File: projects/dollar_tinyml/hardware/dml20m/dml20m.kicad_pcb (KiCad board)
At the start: 2 copper layers, 40 x 20 mm, 37 parts, among them J1 USB_A, J2 Conn_ARM_SWD_TagConnect_TC203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, J3 Header 2.54mm, J4 Header 2.54mm, Q1 BC547B, SW1 SW_Push, U1 LIS2DH12, U2 LP4054HB5F, U3 PY32F003F18U6TR, U4 XC6206PxxxMR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

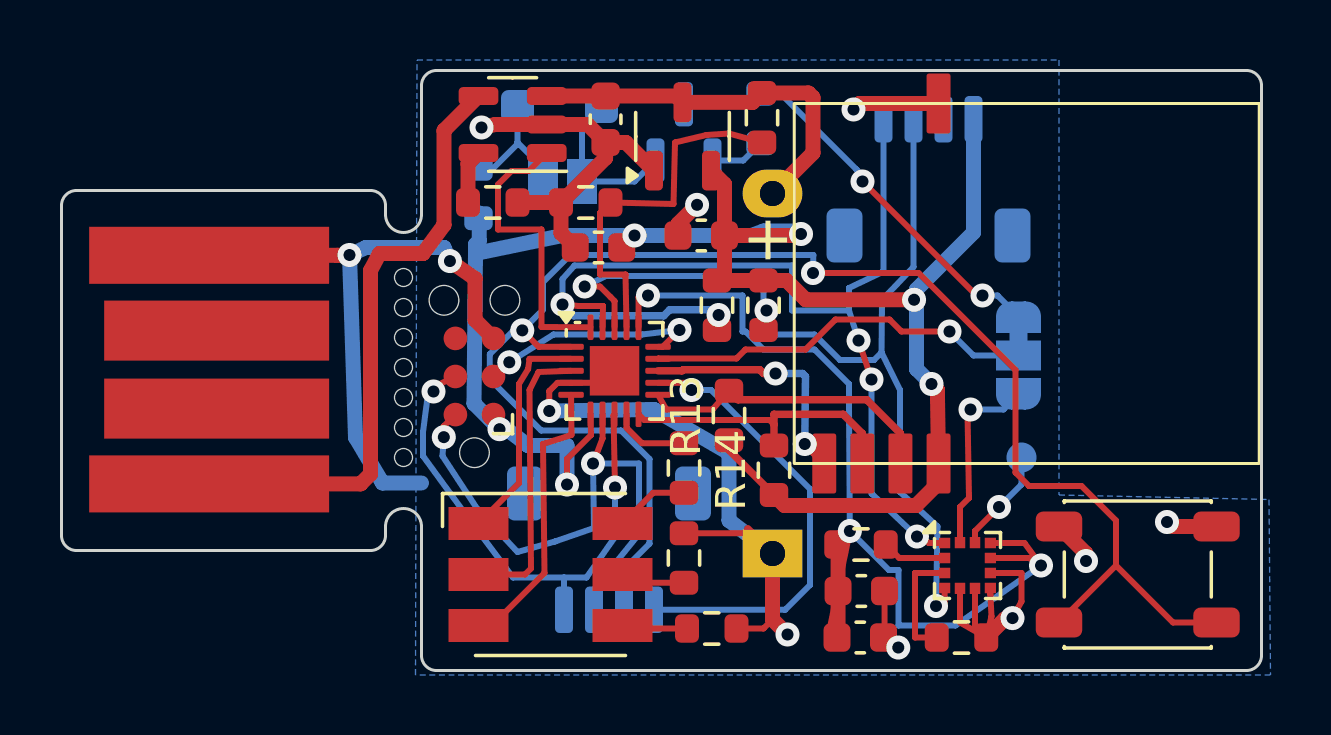
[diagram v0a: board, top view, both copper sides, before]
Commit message: dollarml: Improve groundplane, remove via-in-pad
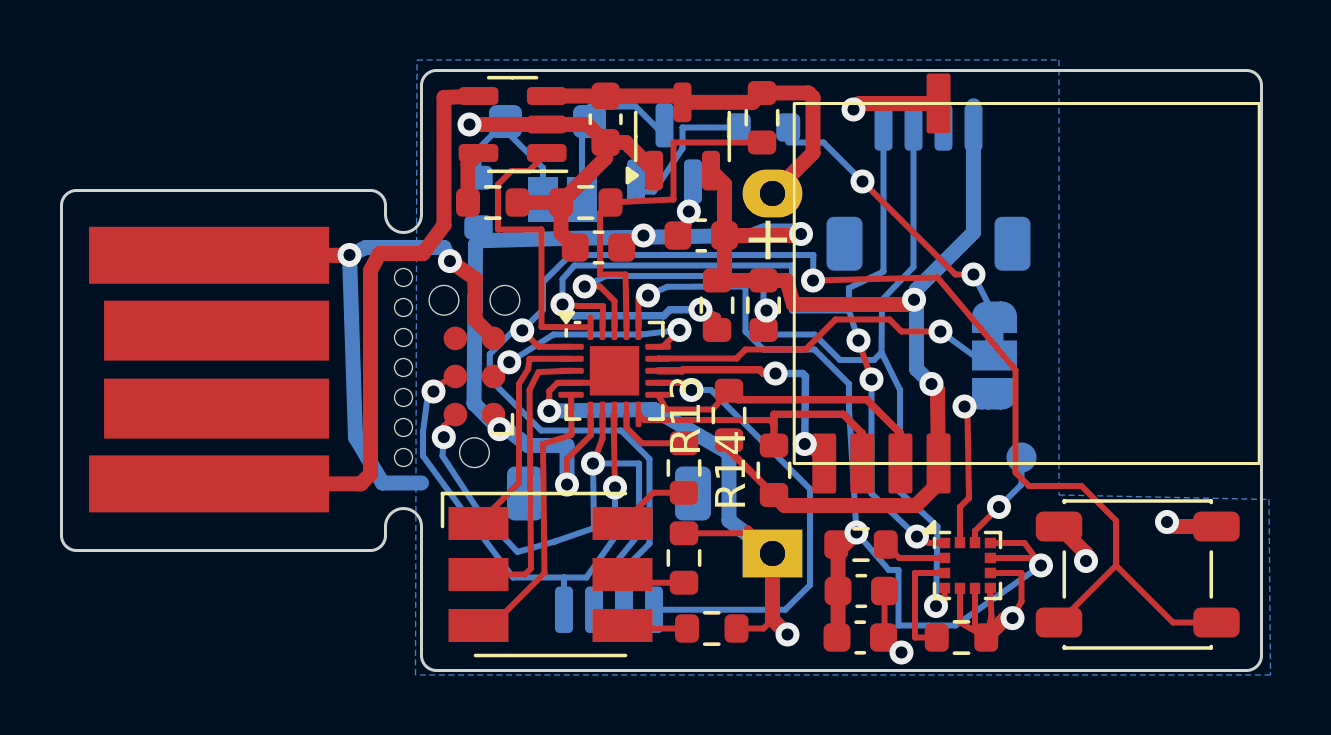
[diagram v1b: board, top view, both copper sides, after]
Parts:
- moved Q1 0.96 mm to (108.1, 92.8)
- moved JP1 0.80 mm to (119.1, 99.5)
- moved D2 0.64 mm to (104.2, 91.7)
- moved BZ1 0.60 mm to (104.7, 94.3)
- moved R11 0.32 mm to (111.4, 91.9), turned to 180 degrees
- moved R12 0.30 mm to (101.9, 94.4)
- moved J4 0.28 mm to (116.9, 93.9)
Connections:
- net Net-(BZ1-+) renamed /BUZZER+
- net Net-(U2-PROG) renamed /BATT_PROG
- BZ1 pad 2: Net-(BZ1--) -> /BUZZER-
- D2 pad 2: Net-(BZ1--) -> /BUZZER-
- Q1 pad 1: Net-(Q1-B) -> GND
- Q1 pad 2: Net-(BZ1--) -> Net-(Q1-B)
- Q1 pad 3: GND -> /BUZZER-
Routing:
- net /BUZZER-: track 0.00 -> 5.77 mm
- net Net-(BZ1--): track 5.51 -> 0.00 mm
- net Net-(Q1-B): track 1.84 -> 4.89 mm
- net /ACC_POWER: track 34.9 -> 32.6 mm
- net /BUZZER: track 11.8 -> 9.76 mm
- net /ACC_INT/BUZZER: track 13.1 -> 11.5 mm
- net GND: track 75.3 -> 76.6 mm
- net VBUS: track 20.3 -> 21.0 mm
- net /ACC_INT1: track 6.41 -> 5.85 mm

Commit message: dollarml: dml20m revision ready for production
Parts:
- BT1: value Battery_Cell -> LIR1225
- D1: value LED_RGB -> LED 5050-6P-GRB
- R11: value 100R -> 120R
- SW1: value SW_Push -> PTS647SM50SMTR2LFS
- U2: value LP4054HB5F -> Li charger 4054
- U4: value XC6206PxxxMR -> XC6206P332MR
- moved J4 0.21 mm to (116.8, 93.7)
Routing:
- net GND: track 76.6 -> 75.4 mm
